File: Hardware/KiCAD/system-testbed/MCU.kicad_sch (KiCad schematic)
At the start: 1 part, among them U5 ESP32-WROVER-E

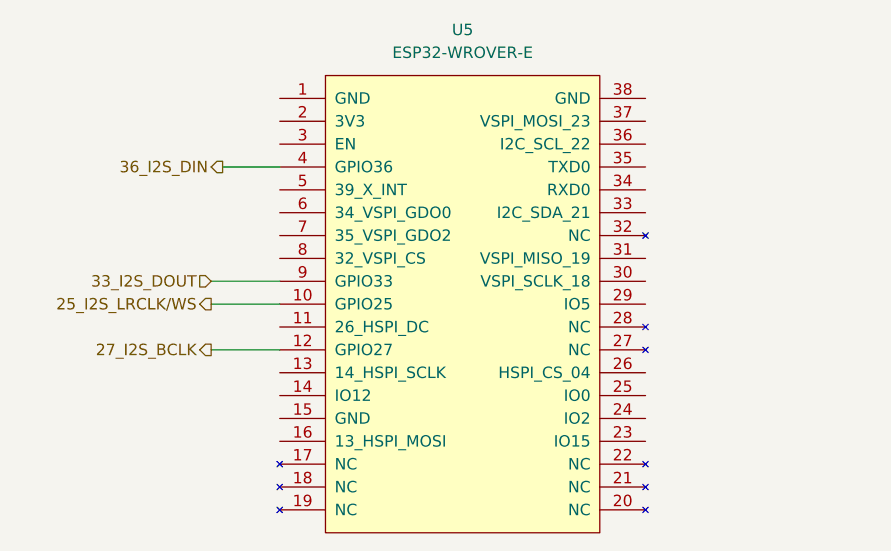
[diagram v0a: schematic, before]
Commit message: feat:  hierarchical labels  #63
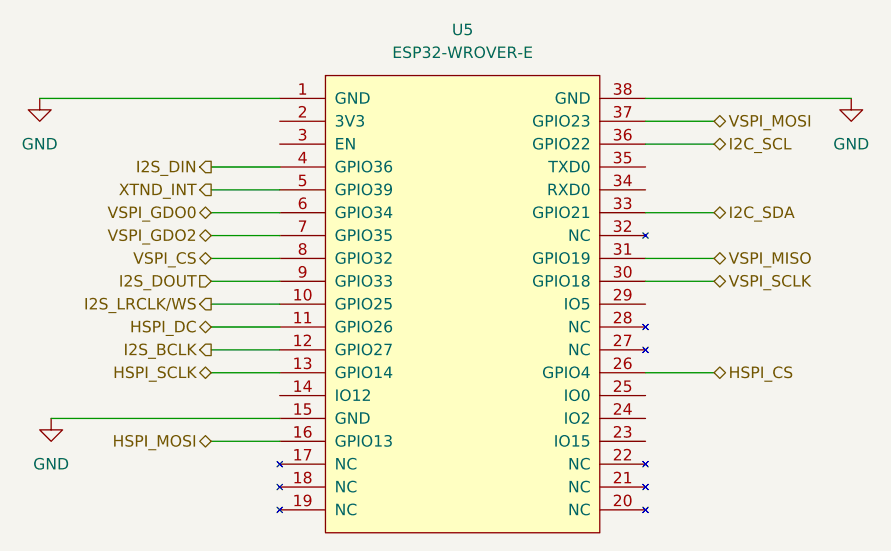
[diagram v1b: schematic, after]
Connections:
- net GND: now reaches U5.1 (GND)
- net GND: now also U5.15 (GND), U5.38 (GND)
- net HSPI_DC: now reaches U5.11 (GPIO26)
- net HSPI_SCLK: now reaches U5.13 (GPIO14)
- net HSPI_MOSI: now reaches U5.16 (GPIO13)
- net HSPI_CS: now reaches U5.26 (GPIO4)
- net VSPI_SCLK: now reaches U5.30 (GPIO18)
- net VSPI_MISO: now reaches U5.31 (GPIO19)
- net I2C_SDA: now reaches U5.33 (GPIO21)
- net I2C_SCL: now reaches U5.36 (GPIO22)
- net VSPI_MOSI: now reaches U5.37 (GPIO23)
- net XTND_INT: now reaches U5.5 (GPIO39)
- net VSPI_GDO0: now reaches U5.6 (GPIO34)
- net VSPI_GDO2: now reaches U5.7 (GPIO35)
- net VSPI_CS: now reaches U5.8 (GPIO32)
- net 25_I2S_LRCLK/WS renamed I2S_LRCLK/WS
- net 27_I2S_BCLK renamed I2S_BCLK
- net 33_I2S_DOUT renamed I2S_DOUT
- net 36_I2S_DIN renamed I2S_DIN

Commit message: feat: schematic capture #63
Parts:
- added C70, C71, C72: C, symbol Device:C
- added R34, R35, R36: R, symbol Device:R
- added SW4: SW_Push, symbol Switch:SW_Push
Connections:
- net GND: now also C70.1, C71.1, C72.1, SW4.1
- net +3.3V: now reaches U5.2 (3V3)
- net +3.3V: now also C70.2, C71.2, R35.2
- net at U5.25 (IO0): now also R36.1
- net at U5.3 (EN): now also C72.2, R34.2, R35.1
- new net: R34.1, SW4.2
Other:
- moved on the sheet: U5

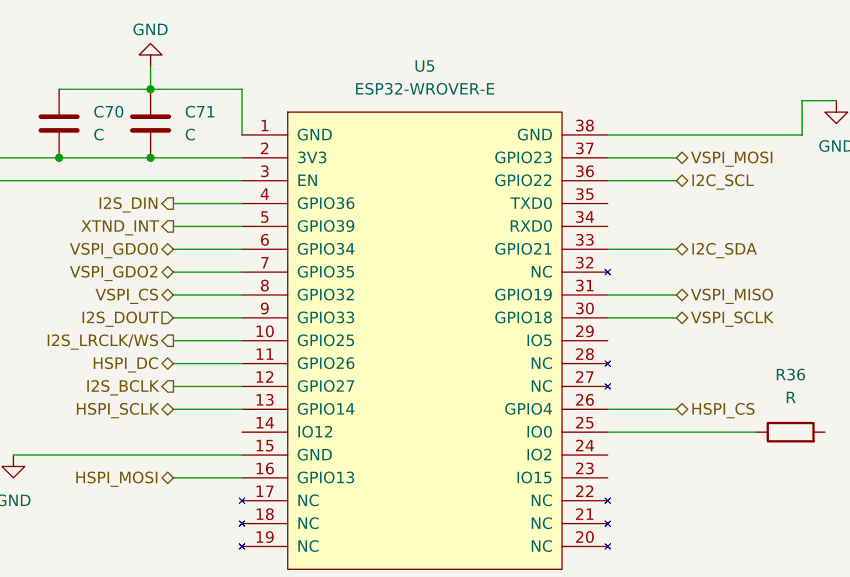
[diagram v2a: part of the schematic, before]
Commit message: feat: added WROVER footprint to project library & symbol
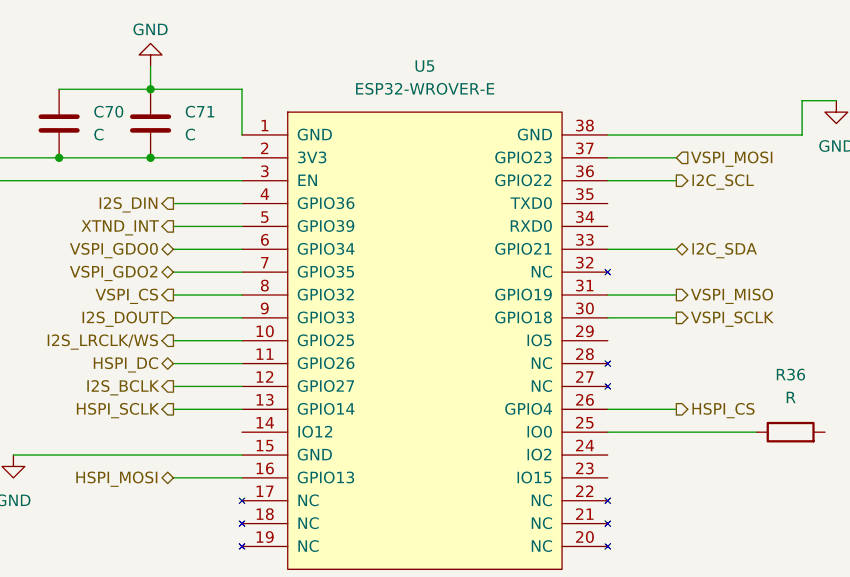
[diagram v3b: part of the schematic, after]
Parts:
- C71: footprint (none) -> Capacitor_SMD:C_0603_1608Metric
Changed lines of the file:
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@@
+	(wire
+		(pts
+			(xy 132.08 106.68) (xy 139.7 106.68)
+		)
+		(stroke
+			(width 0)
+			(type default)
+		)
+	)
 	(wire
 		(pts
@@
 		(pts
 			(xy 132.08 119.38) (xy 139.7 119.38)
-		)
-		(stroke
-			(width 0)
-			(type default)
-		)
-	)
-	(wire
-		(pts
-			(xy 132.08 106.68) (xy 139.7 106.68)
 		)
 		(stroke
@@
 	)
 	(hierarchical_label "VSPI_CS"
-		(shape bidirectional)
+		(shape output)
 		(at 83.82 119.38 180)
 		(effects
@@
 	)
 	(hierarchical_label "HSPI_CS"
-		(shape bidirectional)
+		(shape output)
 		(at 139.7 132.08 0)
 		(effects
@@
 	)
 	(hierarchical_label "VSPI_SCLK"
-		(shape bidirectional)
+		(shape output)
 		(at 139.7 121.92 0)
 		(effects
@@
 	)
 	(hierarchical_label "VSPI_MISO"
-		(shape bidirectional)
+		(shape output)
 		(at 139.7 119.38 0)
 		(effects
@@
 	)
 	(hierarchical_label "HSPI_SCLK"
-		(shape bidirectional)
+		(shape output)
 		(at 83.82 132.08 180)
 		(effects
@@
 		)
 	)
+	(hierarchical_label "I2C_SCL"
+		(shape output)
+		(at 139.7 106.68 0)
+		(effects
+			(font
+				(size 1.27 1.27)
+			)
+			(justify left)
+		)
+	)
 	(hierarchical_label "VSPI_MOSI"
-		(shape bidirectional)
+		(shape input)
 		(at 139.7 104.14 0)
-		(effects
-			(font
-				(size 1.27 1.27)
-			)
-			(justify left)
-		)
-	)
-	(hierarchical_label "I2C_SCL"
-		(shape bidirectional)
-		(at 139.7 106.68 0)
 		(effects
 			(font
@@
 			)
 		)
-		(property "Footprint" ""
+		(property "Footprint" "Capacitor_SMD:C_0603_1608Metric"
 			(at 82.2452 104.14 0)
 			(effects

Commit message: feat: added WROVER footprint to project library & symbol - MCU Schematic capture Fixes #63
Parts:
- U5: footprint (none) -> capstone-project:ESP32-WROVER-IE
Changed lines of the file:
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@@
 			)
 		)
-		(property "Footprint" ""
+		(property "Footprint" "capstone-project:ESP32-WROVER-IE"
 			(at 111.76 115.57 0)
 			(effects
@@
 			)
 		)
-		(property "Datasheet" ""
+		(property "Datasheet" "kicad-embed://esp32-wrover-e_esp32-wrover-ie_datasheet_en.pdf"
 			(at 111.76 115.57 0)
 			(effects
@@
 			)
 		)
-		(property "Description" ""
+		(property "Description" "WROVER-E & WROVER-IE Footprint"
 			(at 111.76 124.46 0)
 			(effects

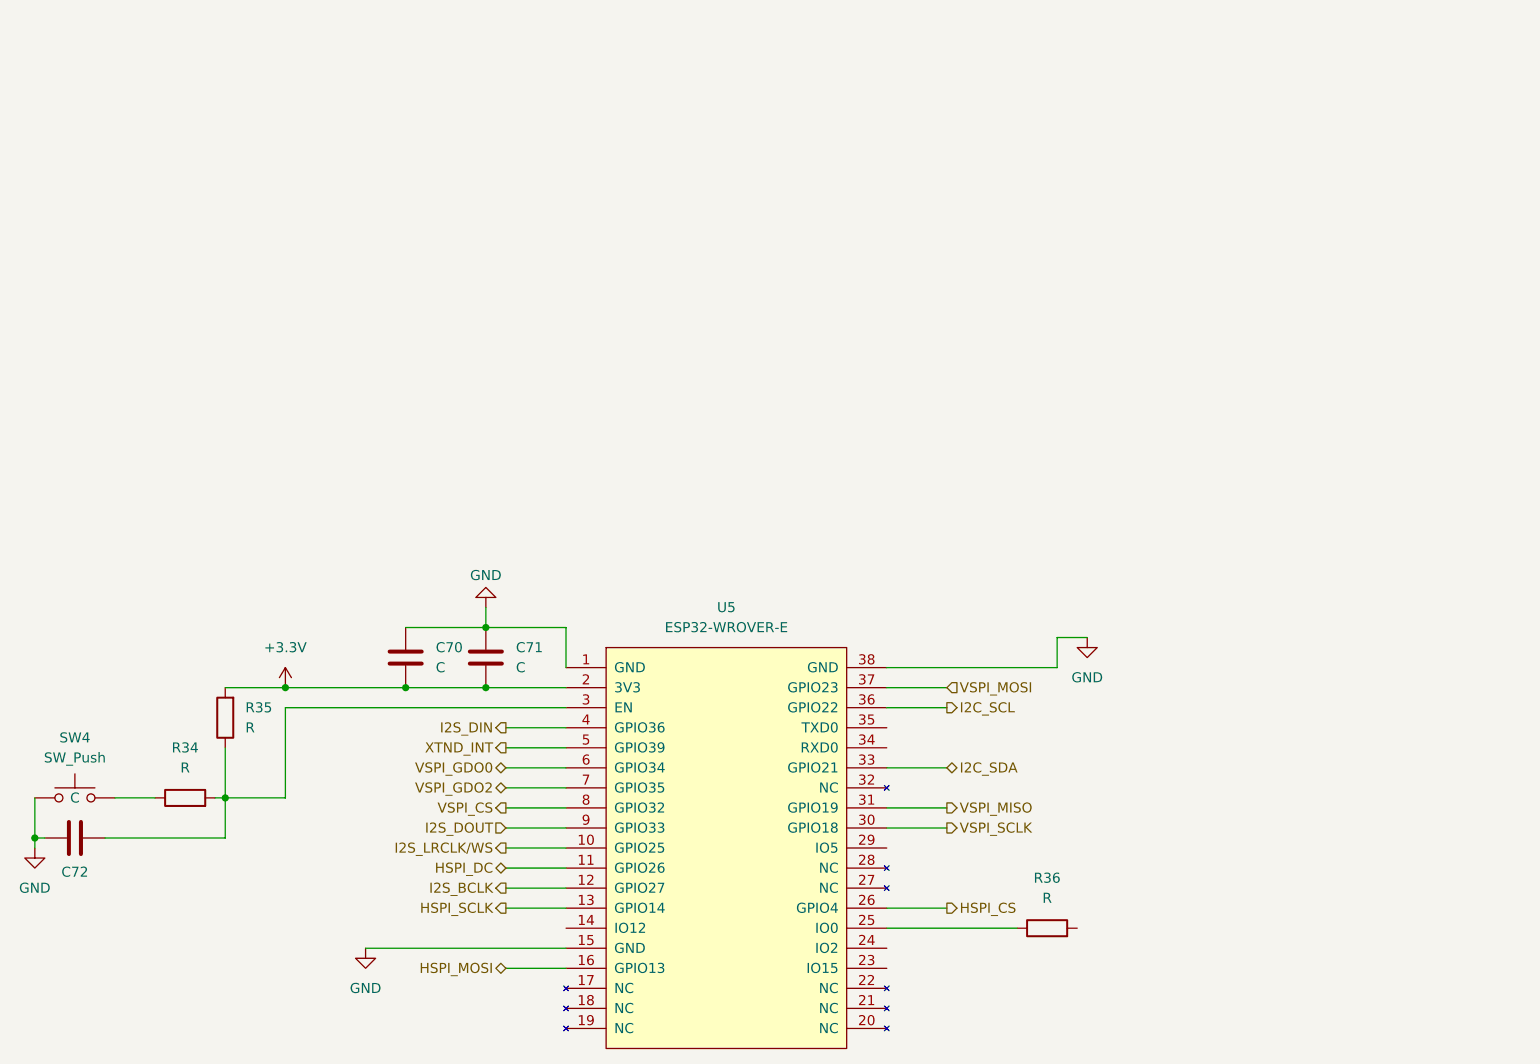
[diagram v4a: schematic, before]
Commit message: feat: MCU changes to root labels & passive component sizes #63
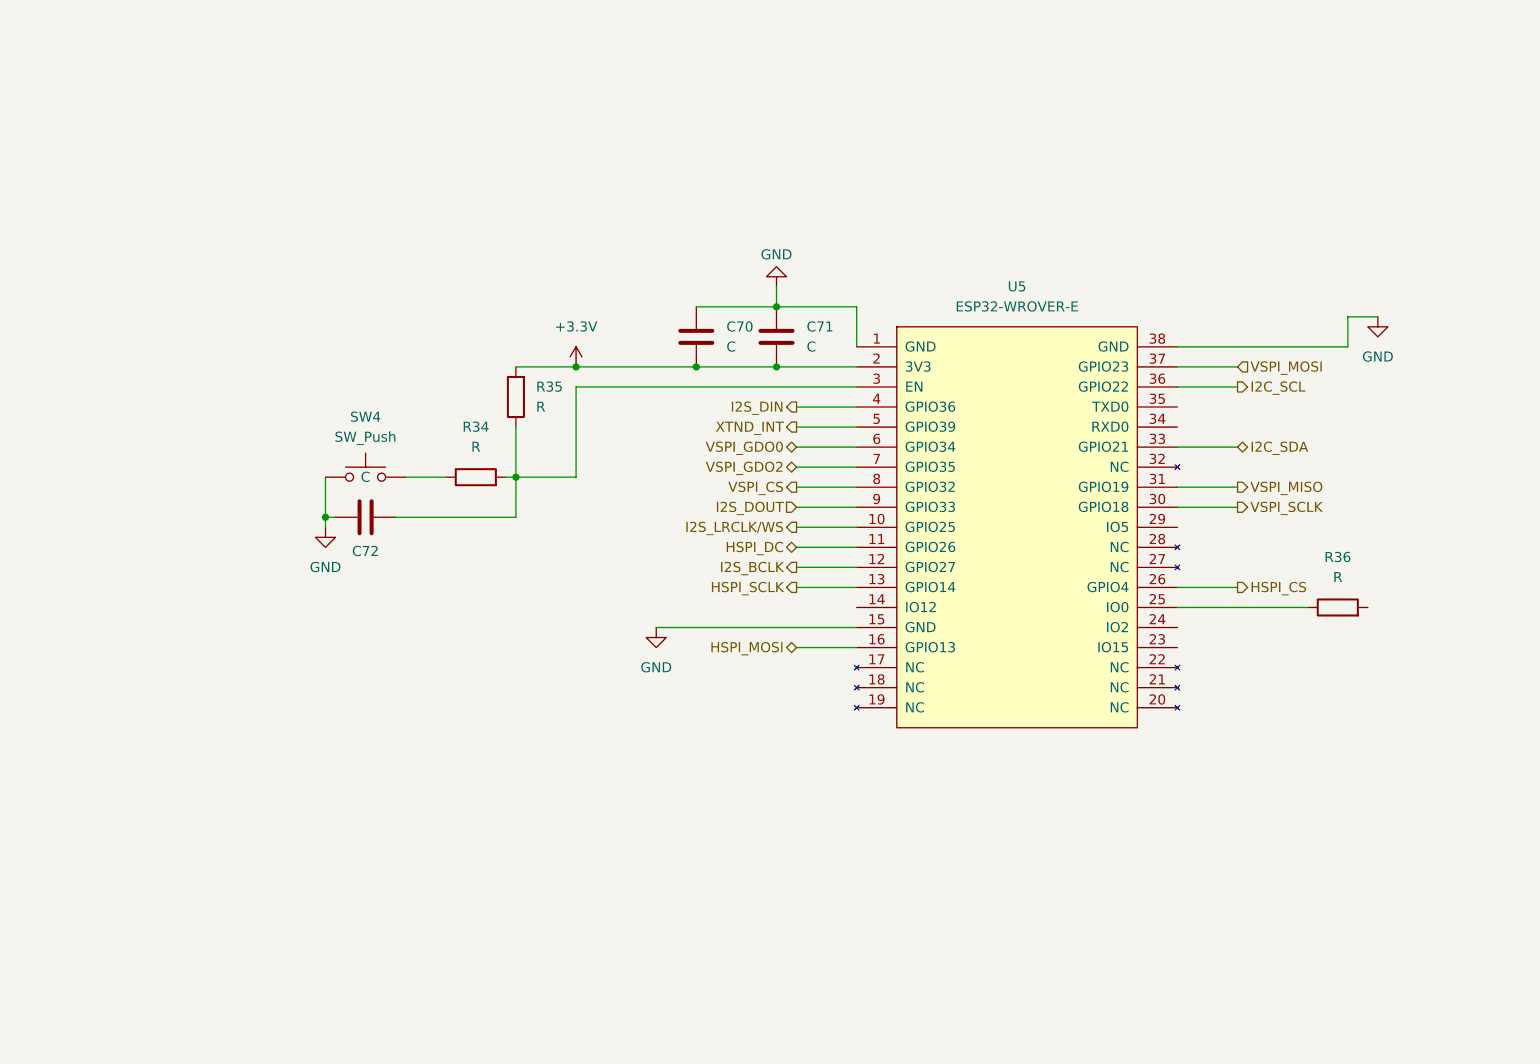
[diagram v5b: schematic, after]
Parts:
- C70, C72: footprint (none) -> Capacitor_SMD:C_0603_1608Metric
- R34, R35, R36: footprint (none) -> Resistor_SMD:R_0603_1608Metric
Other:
- moved on the sheet: C70, C71, C72, R34, R35, R36, SW4, U5

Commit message: fix: recover MCU schematic and esp32 module footprint #60
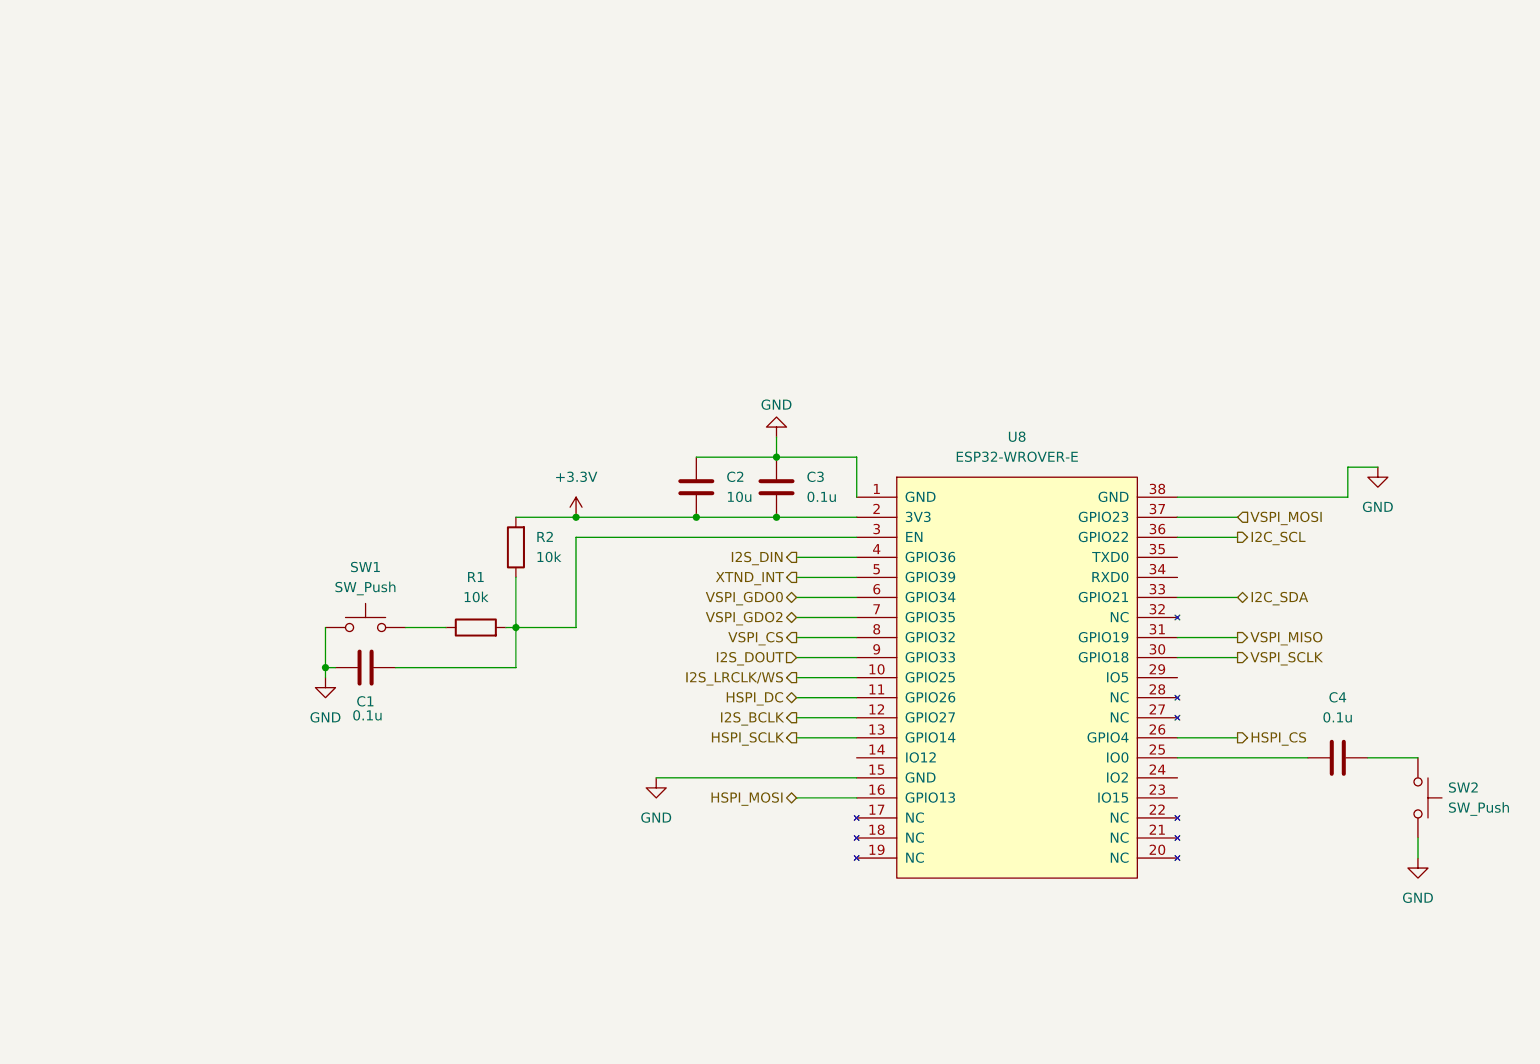
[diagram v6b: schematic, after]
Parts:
- removed C70, C71, C72: C, Capacitor_SMD:C_0603_1608Metric, symbol Device:C
- removed R34, R35, R36: R, Resistor_SMD:R_0603_1608Metric, symbol Device:R
- removed SW4: SW_Push, symbol Switch:SW_Push
- removed U5: ESP32-WROVER-E, capstone-project:ESP32-WROVER-IE, symbol capstone-project:ESP32-WROVER-E
- added C1, C3, C4: 0.1u, Capacitor_SMD:C_0603_1608Metric, symbol Device:C
- added C2: 10u, Capacitor_SMD:C_0603_1608Metric, symbol Device:C
- added R1, R2: 10k, Resistor_SMD:R_0603_1608Metric, symbol Device:R
- added SW1, SW2: SW_Push, Button_Switch_SMD:SW_SPST_EVQP2_MiddlePushTravel_H2.5mm, symbol Switch:SW_Push
- added U8: ESP32-WROVER-E, capstone-project:ESP32-WROVER-IE, symbol capstone-project:ESP32-WROVER-E
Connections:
- net +3.3V: now also C2.2, C3.2, R2.2, U8.2 (3V3)
- net GND: now also C1.1, C2.1, C3.1, SW1.1, SW2.2, U8.1 (GND), U8.15 (GND), U8.38 (GND)
- net HSPI_CS: now also U8.26 (GPIO4)
- net HSPI_DC: now also U8.11 (GPIO26)
- net HSPI_MOSI: now also U8.16 (GPIO13)
- net HSPI_SCLK: now also U8.13 (GPIO14)
- net I2C_SCL: now also U8.36 (GPIO22)
- net I2C_SDA: now also U8.33 (GPIO21)
- net I2S_BCLK: now also U8.12 (GPIO27)
- net I2S_DIN: now also U8.4 (GPIO36)
- net I2S_DOUT: now also U8.9 (GPIO33)
- net I2S_LRCLK/WS: now also U8.10 (GPIO25)
- net VSPI_CS: now also U8.8 (GPIO32)
- net VSPI_GDO0: now also U8.6 (GPIO34)
- net VSPI_GDO2: now also U8.7 (GPIO35)
- net VSPI_MISO: now also U8.31 (GPIO19)
- net VSPI_MOSI: now also U8.37 (GPIO23)
- net VSPI_SCLK: now also U8.30 (GPIO18)
- net XTND_INT: now also U8.5 (GPIO39)
- new net: R1.1, SW1.2
- new net: C1.2, R1.2, R2.1, U8.3 (EN)
- new net: C4.1, U8.25 (IO0)
- new net: C4.2, SW2.1

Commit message: feat: update pinouts for mcu #53
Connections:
- net RXD0: now reaches U8.34 (RXD0)
- net TXD0: now reaches U8.35 (TXD0)
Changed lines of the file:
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@@
+	(wire
+		(pts
+			(xy 176.53 87.63) (xy 168.91 87.63)
+		)
+		(stroke
+			(width 0)
+			(type default)
+		)
+	)
 	(wire
 		(pts
@@
 	(wire
 		(pts
+			(xy 176.53 90.17) (xy 168.91 90.17)
+		)
+		(stroke
+			(width 0)
+			(type default)
+		)
+	)
+	(wire
+		(pts
 			(xy 120.65 95.25) (xy 128.27 95.25)
 		)
@@
 			(width 0)
 			(type default)
+		)
+	)
+	(hierarchical_label "TXD0"
+		(shape output)
+		(at 176.53 87.63 0)
+		(effects
+			(font
+				(size 1.27 1.27)
+			)
+			(justify left)
 		)
 	)
@@
 		(effects
 			(font
+				(size 1.27 1.27)
+			)
+			(justify left)
+		)
+	)
+	(hierarchical_label "RXD0"
+		(shape output)
+		(at 176.53 90.17 0)
+		(effects
+			(font
